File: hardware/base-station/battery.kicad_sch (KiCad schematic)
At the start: 22 parts, among them J2 USB4110GFA, Q1 FS8205A, Q2 FS8205A, Q3 FS8205A, U14 DW01A, U5 BQ21040DBVR

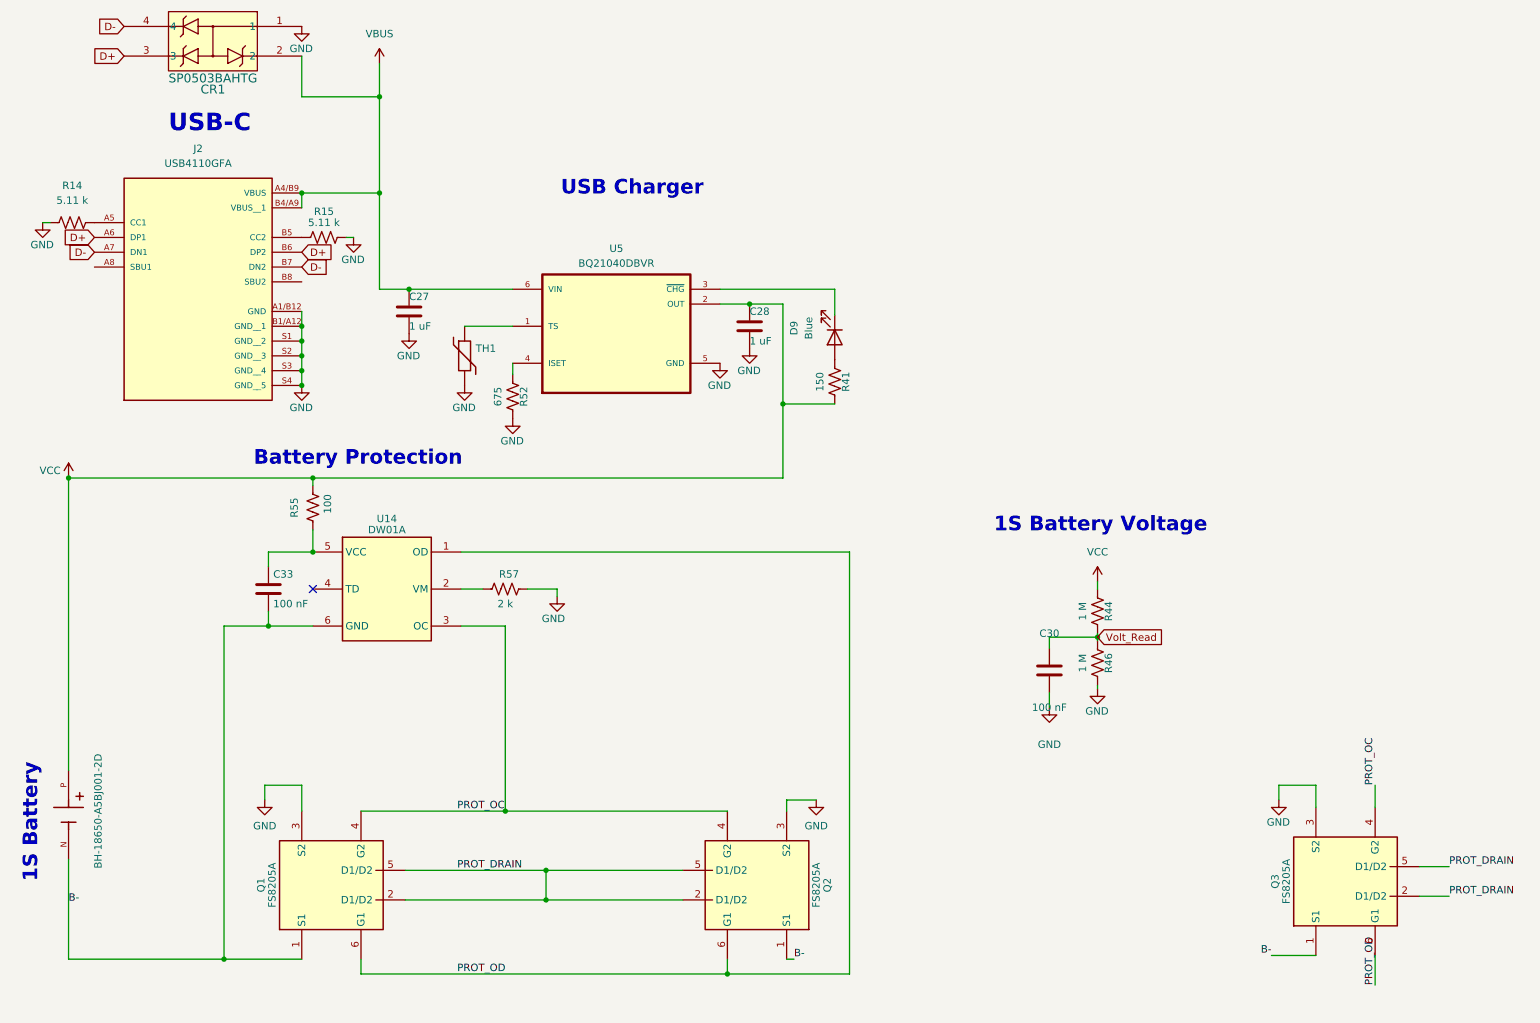
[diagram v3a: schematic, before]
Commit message: hardware: place Q3 and bump C10 to 10 uF on the base-station
Places the third FS8205A whose schematic went in with the previous
commit, so the protection stack is now Q1/Q2/Q3 on the board as well as
on the sheet.

C10 goes 1 uF -> 10 uF. Changed in both esp32_p3.kicad_sch and the
layout, so schematic and board agree.

The battery sheet is rewired - +9 wires, +3 junctions, -5 labels - with
no change to its part set.

Layout otherwise: 38 parts repositioned, 24 track segments removed, 35
vias added, one zone removed.

Co-Authored-By: Claude Opus 5 <noreply@anthropic.com>
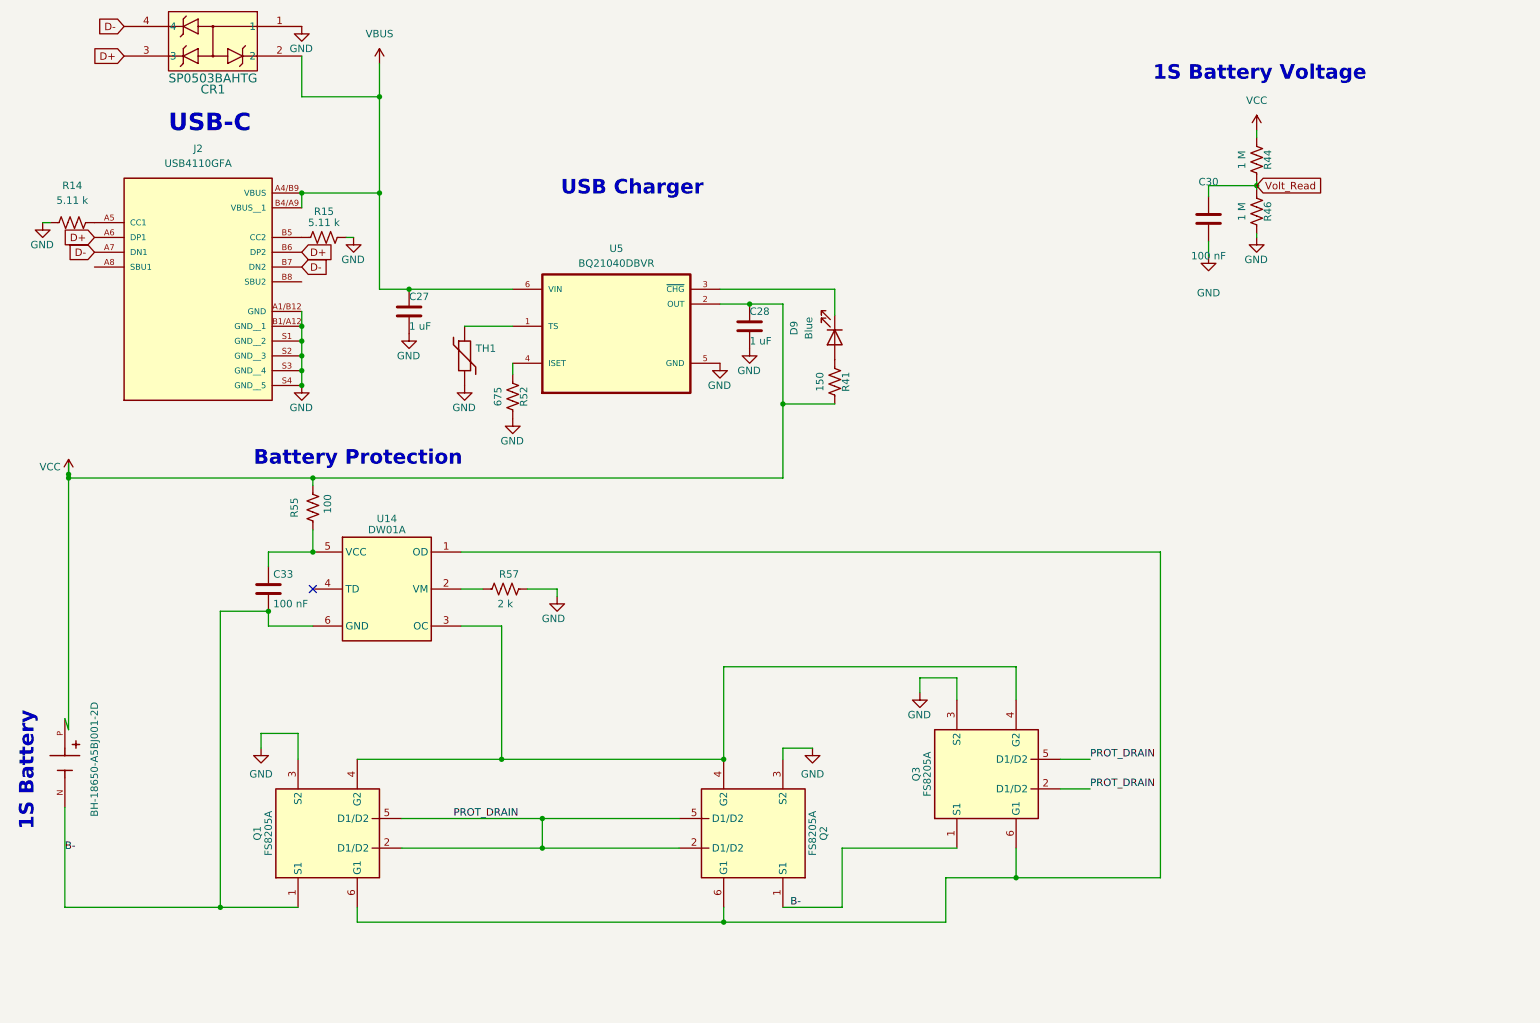
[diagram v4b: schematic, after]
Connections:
- net PROT_OC: no longer names the net of Q1.4 (G2), Q2.4 (G2), Q3.4 (G2), U14.3 (OC)
- net PROT_OD: no longer names the net of Q1.6 (G1), Q2.6 (G1), Q3.6 (G1), U14.1 (OD)
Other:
- moved on the sheet: C30, Q1, Q2, Q3, R44, R46

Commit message: hardware: MPN + Mfr on every purchased part of the three ESP32 boards
Closes the LoRa pre-fab review's finding 3, extended to the sibling boards.
Every non-DNP symbol now names the exact part the cross-board BOM prices, so
the schematic can no longer imply a part that was never quoted.

401 of 401 purchasable parts carry an MPN. The only exemptions are the three
DNP v3.x provisions on the rocket-computer (R74/R75 499 k, R76 0 R): not
fitted, so never purchased, so correctly absent from the BOM.

Values normalised so each part resolves to one BOM line:

  LoRa R74  "10 K" -> "10 k"   capital K split one part across two lines
  LoRa D6   "LED"  -> "Green"  no colour recorded, so no MPN could attach
  Y1/Y3/Y5  "SC-32S-32.768kHz-12.5pF" -> "ABS07-32.768KHZ-T"

Two stale legacy MP fields disagreed with both the Value and the BOM and were
corrected -- a symbol carrying two part numbers is the wrong-part-order hazard
this pass exists to remove:

  rocket U19  TPS259824LNRGER -> ...RGET.  Same die and RGE-24 package; the
              suffix is reel quantity, and power-eco.md documents RGET.
  base   U9   TPS63021DSJR -> TPS63020DSJR.  These are NOT interchangeable:
              63021 is fixed 3.3 V, 63020 is adjustable. U9 pin 3 (FB) drives
              a real divider (R13 1 M / R16 180 k -> 0.5 x (1 + 1M/180k) =
              3.28 V), which only the adjustable part uses. BOM was right.

The ABS07 keeps the existing XTAL_SC-32S_3215 footprint: both parts are
2-pad 3.2 x 1.5 mm tuning forks, so the land is correct and only the
footprint's name now reads for the superseded vendor.

ERC clean on all three boards after the pass.

Co-Authored-By: Claude Opus 5 <noreply@anthropic.com>
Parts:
- BT2: MPN (none) -> BH-18650-A5BJ001-2D; Mfr (none) -> MYOUNG
- C27, C28: MPN (none) -> CL05A105KO5NNNC; Mfr (none) -> Samsung
- C30, C33: MPN (none) -> CL05B104KO5NNNC; Mfr (none) -> Samsung
- CR1: MPN (none) -> SP0503BAHTG; Mfr (none) -> Littelfuse
- D9: MPN (none) -> WP710A10QBC/D; Mfr (none) -> Kingbright
- J2: MPN (none) -> USB4110-GF-A; Mfr (none) -> GCT
- Q1, Q2, Q3: MPN (none) -> FS8205A; Mfr (none) -> TECH PUBLIC
- R14, R15: MPN (none) -> RC0402FR-075K11L; Mfr (none) -> Yageo
- R41: MPN (none) -> RC0402FR-07150RL; Mfr (none) -> Yageo
- R44, R46: MPN (none) -> RC0402FR-071ML; Mfr (none) -> Yageo
- R52: MPN (none) -> RC0402FR-07675RL; Mfr (none) -> Yageo
- R55: MPN (none) -> RC0402FR-07100RL; Mfr (none) -> Yageo
- R57: MPN (none) -> RC0402FR-072KL; Mfr (none) -> Yageo
- TH1: MPN (none) -> 103AT-2; Mfr (none) -> Semitec
- U14: MPN (none) -> DW01A; Mfr (none) -> PUOLOP
- U5: MPN (none) -> BQ21040DBVR; Mfr (none) -> TI

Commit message: hardware(base-station): power-switch review fixes -- MID balance resistors to 1206
Schematic-side only; the PCB has not caught up. Do not fabricate from this
revision.

Review of the base-station power switching (schematic only, this session).
The V5 defect is fixed in this revision: the V_LORA boost is now behind the
TPS22918 load switch, so S1 kills the LoRa daughterboard along with everything
else. Standby with S1 open measures out at ~6 uA typical (DW01A + the 1M/1M
sense divider + leakages), and both chargers stay upstream and fully
functional.

R45/R47 (MP2672A MID cell-balance) 0805 -> 1206, 0.75 W:
  RC0805FR-0760R4L (Yageo, 0.125 W) -> CRCW120660R4FKEAHP (Vishay, 0.75 W)

The pair is 2x 60.4 R in parallel = 30.2 R in the MID balance path. With
R_ON_BHS = 2.1 R (datasheet p9) and the high cell at 4.2 V, balance current is
4.2/32.3 = 130 mA, so each resistor carries 65 mA and burns 65mA^2 * 60.4 =
0.255 W. Balancing runs 249.8 ms of every 250 ms cycle (Figure 13, p24) -- so
that is continuous, not a pulse. The 0805 parts were at 204% of rating; even a
standard 0.25 W 1206 sits at 102%. The Vishay HP part is 0.75 W, i.e. 34%
loaded. Balance current is deliberately unchanged -- this is a power-rating
fix, not a re-tune. Value stays 60.4 R and MPS characterizes the part at
~17 R (p19), so 30.2 R is already the conservative side.

Metadata lockstep on three parts whose values moved but whose MPN fields did
not follow (all caught by the exact MPN-keyed BOM audit):
  R43 10 k    -> RC0402FR-0710KL   (was still the 6.04 k P/N)
  C42 10 uF   -> CL05A106MQ5NUNC   (was still the 1 uF P/N)
  R53 210 k   -> RC0402FR-07210KL  (copy-pasted from R52, kept its 675 R P/N)

R53 is the BQ21040 TS fail-safe: a floating TS does not suspend charging, it
enters TTDM (datasheet 8.4.6), which charges the cell with NTC monitoring,
termination and the 10-hour safety timer all disabled. 210 k holds TS in the
cold-fault window instead. Picked over the datasheet's 237 k because 237 k x
6.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
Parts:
- added R53: 210 k, Resistor_SMD:R_0402_1005Metric, symbol Device:R_US
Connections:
- net GND: now also R53.2
- net at TH1.1, U5.1 (TS): now also R53.1
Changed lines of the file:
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@@
+	)
+	(junction
+		(at 90.17 69.85)
+		(diameter 0)
+		(color 0 0 0 0)
 	)
 	(junction
@@
 	)
 	(junction
+		(at 22.225 95.885)
+		(diameter 0)
+		(color 0 0 0 0)
+	)
+	(junction
 		(at 75.565 30.48)
 		(diameter 0)
@@
 	)
 	(junction
-		(at 22.225 95.885)
-		(diameter 0)
-		(color 0 0 0 0)
-	)
-	(junction
 		(at 62.23 77.47)
 		(diameter 0)
@@
 	(wire
 		(pts
+			(xy 86.995 78.105) (xy 83.185 78.105)
+		)
+		(stroke
+			(width 0)
+			(type default)
+		)
+	)
+	(wire
+		(pts
 			(xy 56.515 108.585) (xy 64.135 108.585)
 		)
@@
 	(wire
 		(pts
-			(xy 22.225 139.065) (xy 21.59 137.16)
-		)
-		(stroke
-			(width 0)
-			(type default)
-		)
-	)
-	(wire
-		(pts
 			(xy 226.06 54.61) (xy 226.06 53.975)
 		)
@@
 	(wire
 		(pts
+			(xy 86.995 69.85) (xy 86.995 78.105)
+		)
+		(stroke
+			(width 0)
+			(type default)
+		)
+	)
+	(wire
+		(pts
 			(xy 21.59 169.545) (xy 48.26 169.545)
 		)
@@
 	(wire
 		(pts
-			(xy 22.225 95.885) (xy 22.225 139.065)
+			(xy 21.59 95.25) (xy 21.59 137.16)
 		)
 		(stroke
@@
 		(pts
 			(xy 64.135 95.885) (xy 22.225 95.885)
+		)
+		(stroke
+			(width 0)
+			(type default)
+		)
+	)
+	(wire
+		(pts
+			(xy 90.17 69.85) (xy 86.995 69.85)
+		)
+		(stroke
+			(width 0)
+			(type default)
+		)
+	)
+	(wire
+		(pts
+			(xy 21.59 95.25) (xy 22.225 95.885)
 		)
 		(stroke
@@
 				(path "/d2421514-d142-4c71-ac69-48d30c1a771f/2379f198-28b9-4984-b470-63cb7f5b1a0e"
 					(reference "#PWR062")
+					(unit 1)
+				)
+			)
+		)
+	)
+	(symbol
+		(lib_id "power:GND")
+		(at 83.185 85.725 0)
+		(unit 1)
+		(body_style 1)
+		(exclude_from_sim no)
+		(in_bom yes)
+		(on_board yes)
+		(in_pos_files yes)
+		(dnp no)
+		(property "Reference" "#PWR067"
+			(at 83.185 92.075 0)
+			(hide yes)
+			(show_name no)
+			(do_not_autoplace no)
+			(effects
+				(font
+					(size 1.27 1.27)
+				)
+			)
+		)
+		(property "Value" "GND"
+			(at 85.09 89.535 0)
+			(show_name no)
+			(do_not_autoplace no)
+			(effects
+				(font
+					(size 1.27 1.27)
+				)
+				(justify right)
+			)
+		)
+		(property "Footprint" ""
+			(at 83.185 85.725 0)
+			(hide yes)
+			(show_name no)
+			(do_not_autoplace no)
+			(effects
+				(font
+					(size 1.27 1.27)
+				)
+			)
+		)
+		(property "Datasheet" ""
+			(at 83.185 85.725 0)
+			(hide yes)
+			(show_name no)
+			(do_not_autoplace no)
+			(effects
+				(font
+					(size 1.27 1.27)
+				)
+			)
+		)
+		(property "Description" ""
+			(at 83.185 85.725 0)
+			(hide yes)
+			(show_name no)
+			(do_not_autoplace no)
+			(effects
+				(font
+					(size 1.27 1.27)
+				)
+			)
+		)
+		(pin "1"
+		)
+		(instances
+			(project "base-station"
+				(path "/d2421514-d142-4c71-ac69-48d30c1a771f/2379f198-28b9-4984-b470-63cb7f5b1a0e"
+					(reference "#PWR067")
 					(unit 1)
 				)
@@
 					(unit 1)
 				)
+			)
+		)
+	)
+	(symbol
+		(lib_id "Device:R_US")
+		(at 83.185 81.915 0)
+		(unit 1)
+		(body_style 1)
+		(exclude_from_sim no)
+		(in_bom yes)
+		(on_board yes)
+		(in_pos_files yes)
+		(dnp no)
+		(property "Reference" "R53"
+			(at 85.09 81.915 90)
+			(show_name no)
+			(do_not_autoplace no)
+			(effects
+				(font
+					(size 1.27 1.27)
+				)
+			)
+		)
+		(property "Value" "210 k"
+			(at 80.645 81.915 90)
+			(show_name no)
+			(do_not_autoplace no)
+			(effects
+				(font
+					(size 1.27 1.27)
+				)
+			)
+		)
+		(property "Footprint" "Resistor_SMD:R_0402_1005Metric"
+			(at 84.201 82.169 90)
+			(hide yes)
+			(show_name no)
+			(do_not_autoplace no)
+			(effects
+				(font
+					(size 1.27 1.27)
+				)
+			)
+		)
+		(property "Datasheet" ""
+			(at 83.185 81.915 0)
+			(hide yes)
+			(show_name no)
+			(do_not_autoplace no)
+			(effects
+				(font
+					(size 1.27 1.27)
+				)
+			)
+		)
+		(property "Description" ""
+			(at 83.185 81.915 0)
+			(hide yes)
+			(show_name no)
+			(do_not_autoplace no)
+			(effects
+				(font
+					(size 1.27 1.27)
+				)
+			)
+		)
+		(property "MPN" "RC0402FR-07210KL"
+			(at 83.185 81.915 0)
+			(hide yes)
+			(show_name no)
+			(do_not_autoplace no)
+			(effects
+				(font
+					(size 1.27 1.27)
+				)
+			)
+		)
+		(property "Mfr" "Yageo"
+			(at 83.185 81.915 0)
+			(hide yes)
+			(show_name no)
+			(do_not_autoplace no)
+			(effects
+				(font
+					(size 1.27 1.27)
+				)
+			)
+		)
+		(pin "1"
+		)
+		(pin "2"
+		)
+		(instances
+			(project "base-station"
+				(path "/d2421514-d142-4c71-ac69-48d30c1a771f/2379f198-28b9-4984-b470-63cb7f5b1a0e"
+					(reference "R53")
+					(unit 1)
+				)

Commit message: hardware(base-station): pre-fab fixes -- JLC stackup, RF feed, R17/R18, EN margin
The board changes the 2026-08-02 pre-manufacturing review called for. Board is
DRC-clean: 0 errors, 0 unconnected items, 0 schematic-parity issues.

Electrical:
- R17 10 k -> 18.7 k and R18 1 k, both with MPNs that match their values. Both
  previously carried RC0402FR-075K11L (5.11 k). Built to that MPN the TPS61023
  EN pin would sit at 1.65 V driven low, above the 1.2 V V_EN_H ceiling, and the
  LoRa power-cycle recovery would never work with no symptom. 18.7 k/1 k gives
  0.174 V against the 0.35 V guaranteed-low floor, and is already a fleet MPN so
  it adds no BOM line.
- Antenna matching reduced to Molex section 6.0: L4 4.3 nH shunt alone, with
  C2 = 0 ohm realised as a direct trace. C25/C26/L7 removed. The previous
  four-element network put 4.3 nH in parallel with 1.5 pF, which is -j127.8 ohm
  at 2.44 GHz where the Molex reference is +j65.9 ohm -- a sign inversion, not a
  value shift. Accepted trade: this build has no tuning provision, so it must be
  characterised with the cell installed and the result carried into the next
  revision.
- U15 fixing pads 1-3 left individually unconnected. AS-479480001 calls them
  fixing pads and never specifies their net; grounding them is an unforced risk
  on an LDS part whose plating wraps the body.

Stackup and rules, now JLCPCB standard 4-layer:
- JLC04161H-7628: 0.2104 mm 7628 prepreg (Er 4.4), 0.5 oz inner copper, 1.065 mm
  core, ENIG, 1.5862 mm. The previous 0.1 mm prepreg and 1 oz inner layers were
  not a stackup any standard 4-layer order builds.
- RF feed re-solved for the new dielectric: 0.20 -> 0.36 mm, giving 49.7 ohm as
  CPWG at the 0.15 mm pour gap. At 0.20 mm on the new stackup it would have been
  ~68 ohm. New RF netclass carries the width and clearance.
- min_clearance 0.09 -> 0.10 (0.09 falls in the JLC 3.0-3.5 mil upcharge band),
  min_via_diameter 0.40 -> 0.45, annular 0.05 -> 0.075, drill 0.1 -> 0.3, silk
  text 0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
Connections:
- net VCC: no longer R44.1
- new net V_SWITCH: R44.1
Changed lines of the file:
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@@
 	(text "1S Battery Voltage"
 		(exclude_from_sim no)
-		(at 208.28 27.94 0)
+		(at 208.28 21.59 0)
 		(effects
 			(font
@@
 				)
 				(justify right)
+			)
+		)
+	)
+	(global_label "V_SWITCH"
+		(shape input)
+		(at 226.06 36.195 90)
+		(fields_autoplaced yes)
+		(effects
+			(font
+				(size 1.27 1.27)
+			)
+			(justify left)
+		)
+		(property "Intersheetrefs" "${INTERSHEET_REFS}"
+			(at 226.06 24.3198 90)
+			(hide yes)
+			(show_name no)
+			(do_not_autoplace no)
+			(effects
+				(font
+					(size 1.27 1.27)
+				)
+				(justify left)
 			)
 		)
@@
 					(unit 1)
 				)
-			)
-		)
-	)
-	(symbol
-		(lib_id "power:VCC")
-		(at 226.06 36.195 0)
-		(unit 1)
-		(body_style 1)
-		(exclude_from_sim no)
-		(in_bom yes)
-		(on_board yes)
-		(in_pos_files yes)
-		(dnp no)
-		(fields_autoplaced yes)
-		(property "Reference" "#PWR047"
-			(at 226.06 40.005 0)
-			(hide yes)
-			(show_name no)
-			(do_not_autoplace no)
-			(effects
-				(font
-					(size 1.27 1.27)
-				)
-			)
-		)
-		(property "Value" "VCC"
-			(at 226.06 31.115 0)
-			(show_name no)
-			(do_not_autoplace no)
-			(effects
-				(font
-					(size 1.27 1.27)
-				)
-			)
-		)
-		(property "Footprint" ""
-			(at 226.06 36.195 0)
-			(hide yes)
-			(show_name no)
-			(do_not_autoplace no)
-			(effects
-				(font
-					(size 1.27 1.27)
-				)
-			)
-		)
-		(property "Datasheet" ""
-			(at 226.06 36.195 0)
-			(hide yes)
-			(show_name no)
-			(do_not_autoplace no)
-			(effects
-				(font
-					(size 1.27 1.27)
-				)
-			)
-		)
-		(property "Description" "Power symbol creates a global label with name \"VCC\""
-			(at 226.06 36.195 0)
-			(hide yes)
-			(show_name no)
-			(do_not_autoplace no)
-			(effects
-				(font
-					(size 1.27 1.27)
-				)
-			)
-		)
-		(pin "1"
-		)
-		(instances
-			(project "base-station"
-				(path "/d2421514-d142-4c71-ac69-48d30c1a771f/2379f198-28b9-4984-b470-63cb7f5b1a0e"
-					(reference "#PWR047")
-					(unit 1)
-				)

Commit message: hardware(base-station): R52 ISET 675 -> 680 -- the 675 MPN does not exist
R52 sets the BQ21040 charge current (ICHG = 540 AOhm / R). 675 ohm is
TI's own datasheet value for the 0.8 A maximum, but it is not an E24/
E96/E192 value and the pattern-generated RC0402FR-07675RL is not an
orderable part. 680 ohm (RC0402FR-07680RL, E24, deep stock) gives
794 mA -- 0.8% under target, inside the BQ21040's +/-10% ISET accuracy.
No firmware impact (hardware-set current). bom.csv regenerated; ERC/DRC
profiles unchanged.

Co-Authored-By: Claude Fable 5 <noreply@anthropic.com>
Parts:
- R52: value 675 -> 680; MPN RC0402FR-07675RL -> RC0402FR-07680RL
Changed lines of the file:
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@@
 			)
 		)
-		(property "Value" "675"
+		(property "Value" "680"
 			(at 95.885 81.915 90)
 			(show_name no)
@@
 			)
 		)
-		(property "MPN" "RC0402FR-07675RL"
+		(property "MPN" "RC0402FR-07680RL"
 			(at 98.425 81.915 0)
 			(hide yes)
